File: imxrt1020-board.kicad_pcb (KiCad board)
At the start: 2 copper layers, 102.9 x 68.6 mm, 168 parts, among them J1 Micro_SD_Card_Det, J10 CASTELATED, J11 CASTELATED, J12 CASTELATED, J13 CASTELATED, J14 CASTELATED, J15 CASTELATED, J16 CASTELATED, J17 CASTELATED, J18 CASTELATED, J19 CASTELATED, J2 USB_OTG, J20 CASTELATED, J21 CASTELATED, J22 CASTELATED, J23 CASTELATED, J24 CASTELATED, J25 CASTELATED, J26 CASTELATED, J27 CASTELATED, J28 CASTELATED, J29 CASTELATED, J3 Conn_02x20_Odd_Even, J30 CASTELATED, J31 CASTELATED, J32 CASTELATED, J33 CASTELATED, J34 CASTELATED, J35 CASTELATED, J36 CASTELATED, J37 CASTELATED, J38 CASTELATED, J39 CASTELATED, J4 CASTELATED, J40 CASTELATED, J41 CASTELATED, J42 CASTELATED, J43 CASTELATED, J44 GS2, J45 GS2, J46 PWR_IN, J47 JTAG, J48 Conn_01x05, J49 CASTELATED, J5 CASTELATED, J50 CASTELATED, J51 CASTELATED, J52 CASTELATED, J53 CASTELATED, J54 CASTELATED, J55 CASTELATED, J56 CASTELATED, J57 CASTELATED, J58 RJ45-TRANSFO, J59 CASTELATED, J6 CASTELATED, J60 CASTELATED, J61 CASTELATED, J62 CASTELATED, J63 CASTELATED, J64 CASTELATED, J65 CASTELATED, J66 CASTELATED, J7 CASTELATED, J8 CASTELATED, J9 CASTELATED, SW1 RST, SW2 SW_DIP_x02, U1 imx_rt1020-qfp144, U2 M25PX32-VMW, U3 AS4C16M16S, U4 TPS3839DBZ, U5 LM1084-3.3, U6 ISL3178E, U7 KSZ8081RNA, U8 TCAN332D, Y1 24MHz, Y2 32.768Khz

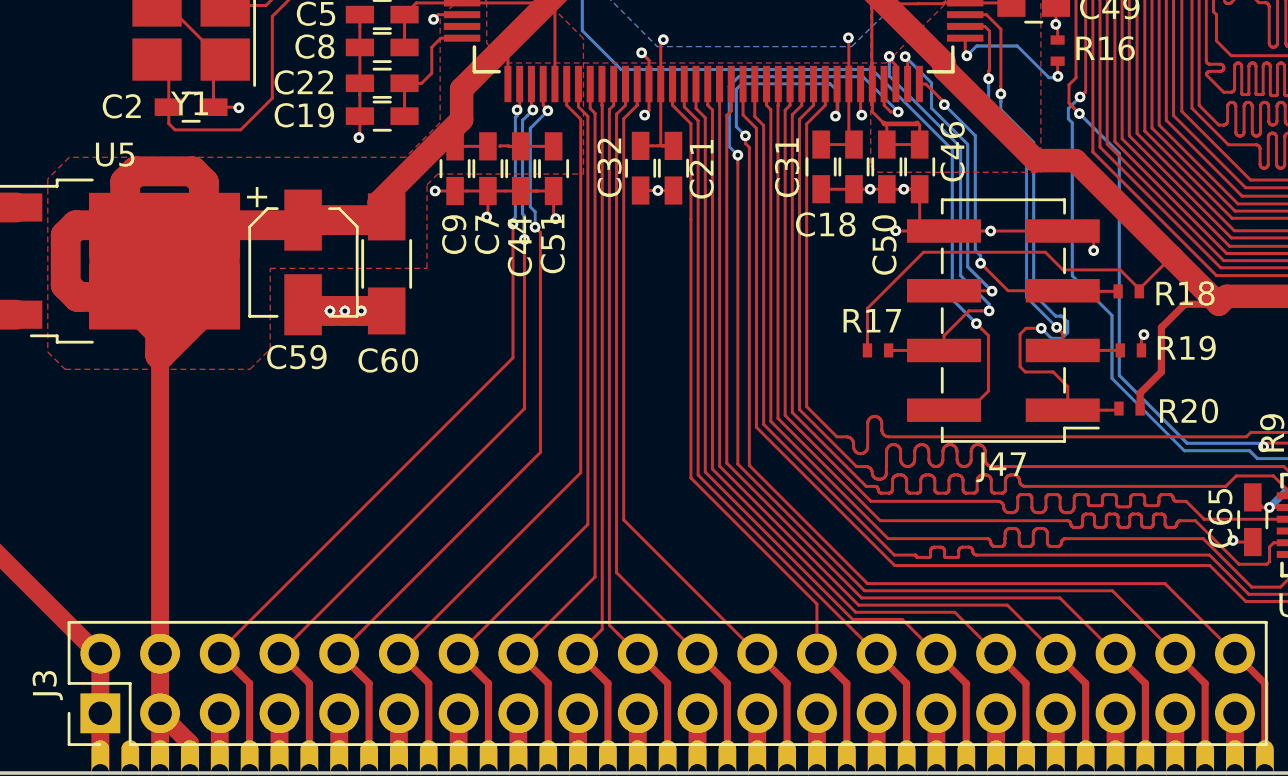
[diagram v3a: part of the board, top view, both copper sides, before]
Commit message: Add GPIO legends (in progress)
Signed-off-by: Martin Ribelotta <martinribelotta@gmail.com>
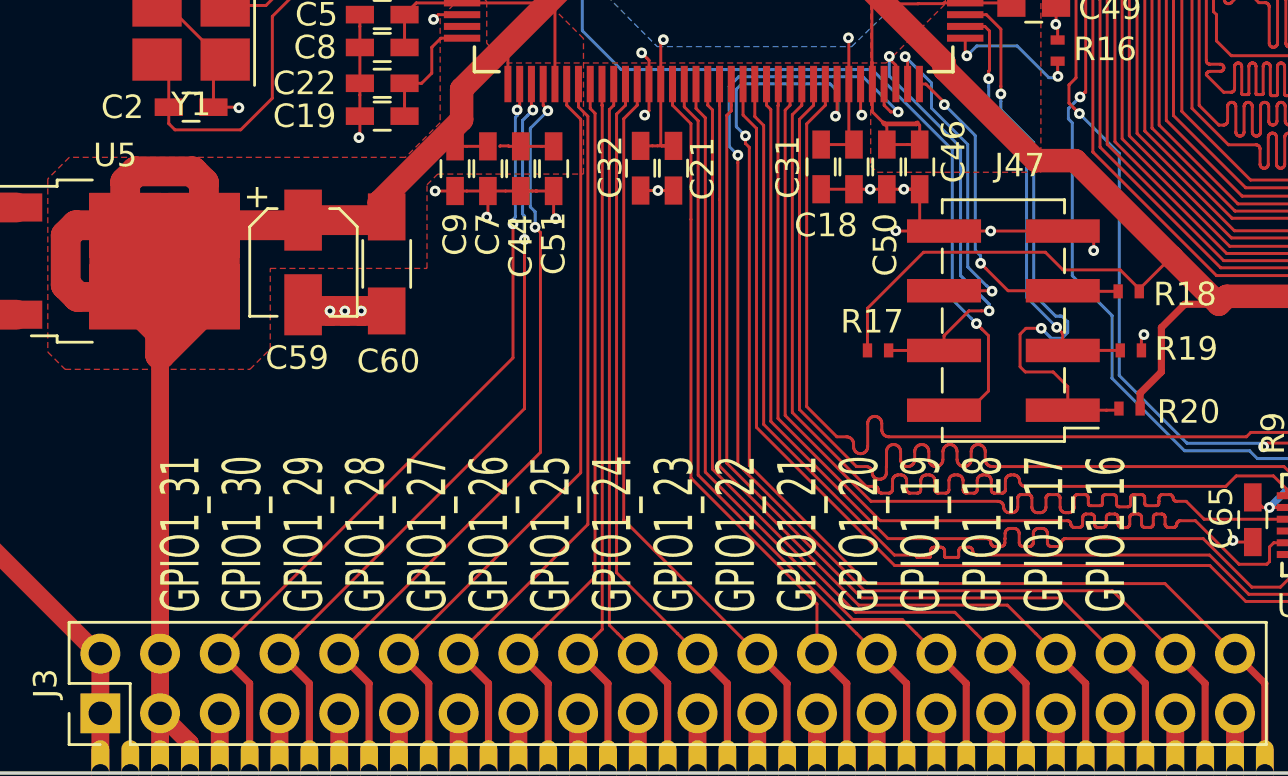
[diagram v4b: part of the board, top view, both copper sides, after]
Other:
- board text added: "GPIO1_31 GPIO1_30 GPIO1_29 GPIO1_28 GPIO1_27 GPIO1_26 GPIO1_25 GPIO1_24 GPIO1_23 GPIO1_22 GPIO1_21 GPIO1_20 GPIO1_19 GPIO1_18 GPIO1_17 GPIO1_16"
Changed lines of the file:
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@@
     (links 461)
     (no_connects 3)
-    (area 107.697199 71.171999 210.72504 139.902001)
+    (area 101.0666 68.199 237.5295 160.624501)
     (thickness 1.6)
-    (drawings 6)
+    (drawings 7)
     (tracks 15178)
     (zones 0)
@@
     (tags "Surface mounted pin header SMD 2x04 2.54mm double row")
     (attr smd)
-    (fp_text reference J47 (at 0 -6.14 180) (layer F.SilkS)
+    (fp_text reference J47 (at -0.69366 6.60146 180) (layer F.SilkS)
       (effects (font (size 1 1) (thickness 0.15)))
     )
@@
     )
   )
+  (gr_text "GPIO1_31\nGPIO1_30\nGPIO1_29\nGPIO1_28\nGPIO1_27\nGPIO1_26\nGPIO1_25\nGPIO1_24\nGPIO1_23\nGPIO1_22\nGPIO1_21\nGPIO1_20\nGPIO1_19\nGPIO1_18\nGPIO1_17\nGPIO1_16\n" (at 151.1935 129.667 90) (layer F.SilkS)
+    (effects (font (size 1.63 1) (thickness 0.25)))
+  )
   (dimension 68.58 (width 0.3) (layer Eco2.User)

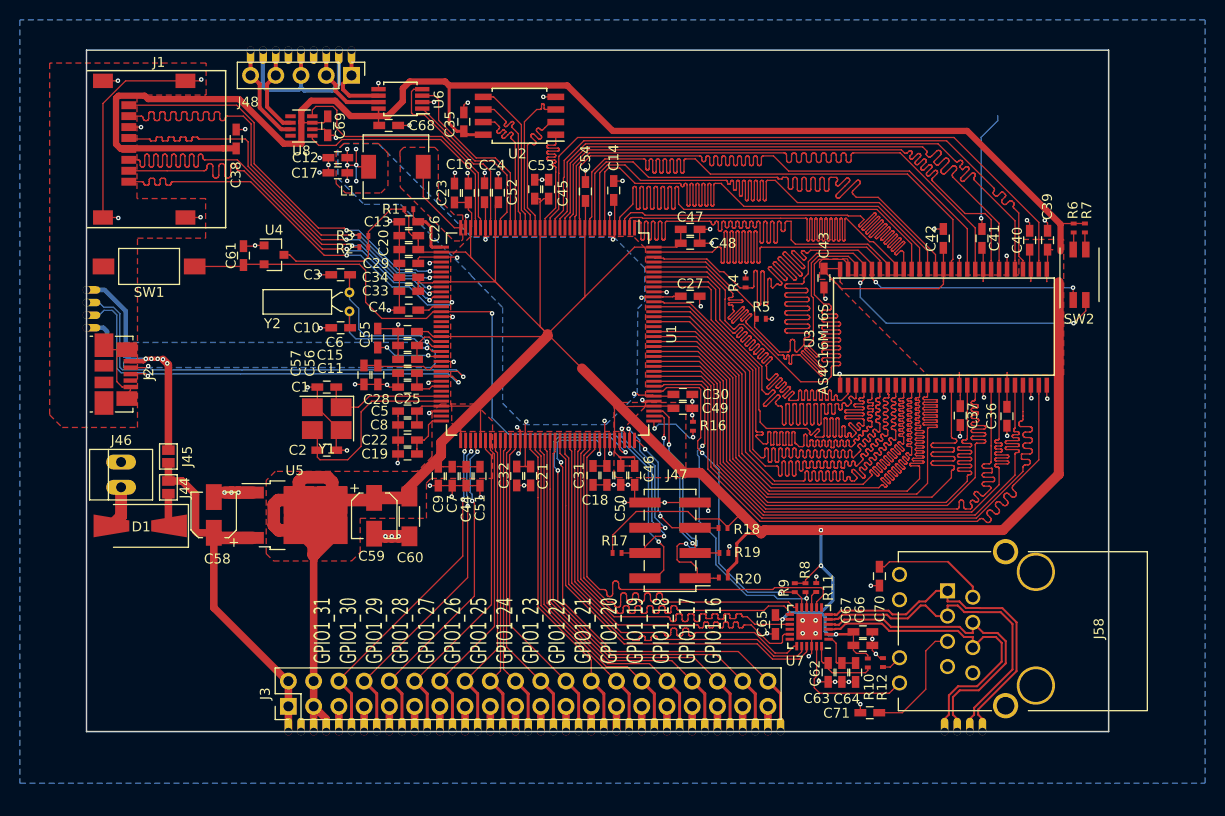
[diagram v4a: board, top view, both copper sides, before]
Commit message: Add WAKE button and GPIO leds, enance GND connections
Signed-off-by: Martin Ribelotta <martinribelotta@gmail.com>
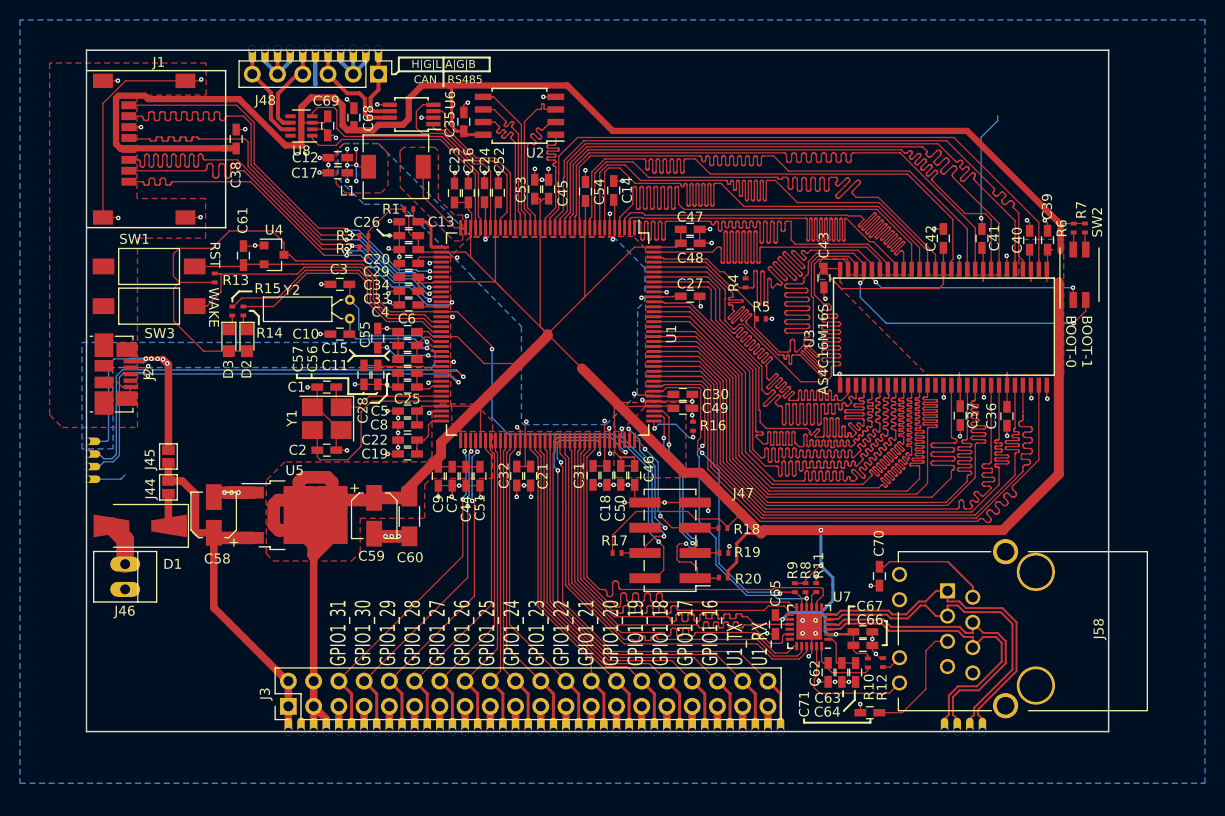
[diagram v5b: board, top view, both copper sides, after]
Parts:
- added D2: RED, LEDs:LED_0805, F.Cu at (123.9, 100.4)
- added D3: RED, LEDs:LED_0805, F.Cu at (122.1, 100.4)
- added J67: CASTELATED, local:castelated_pad, F.Cu at (134.6, 71.1)
- added J68: CASTELATED, local:castelated_pad, F.Cu at (135.9, 71.1)
- added R13: 10K, Resistors_SMD:R_0402_NoSilk, F.Cu at (120.7, 94.2)
- added R14: 220R, Resistors_SMD:R_0402_NoSilk, F.Cu at (123.6, 97.5)
- added R15: 220R, Resistors_SMD:R_0402_NoSilk, F.Cu at (122.4, 97.5)
- added SW3: WAKE, Buttons_Switches_SMD:SW_SPST_FSMSM, F.Cu at (114.1, 97.0)
- J48: value Conn_01x05 -> Conn_01x06; footprint Pin_Headers:Pin_Header_Straight_1x05_Pitch2.54mm -> Pin_Headers:Pin_Header_Straight_1x06_Pitch2.54mm
- moved J65 15.2 mm to (107.8, 110.6)
- moved J66 15.2 mm to (107.8, 114.4)
- moved J63 15.2 mm to (107.8, 113.2)
- moved J64 15.2 mm to (107.8, 111.9)
- moved J46 7.75 mm to (111.7, 123.0), turned to 270 degrees
- moved C68 3.59 mm to (134.7, 78.0), turned to 90 degrees
- moved J49 2.72 mm to (129.5, 71.1)
- moved J48 2.72 mm to (137.2, 73.7)
- moved J55 2.72 mm to (137.2, 71.1)
- moved U6 1.93 mm to (140.5, 77.7)
- moved J52 1.10 mm to (127.0, 71.1)
- moved J53 1.10 mm to (128.3, 71.1)
- moved C3 0.97 mm to (133.3, 94.8)
- moved Y2 0.74 mm to (134.3, 96.4)
- moved C10 0.64 mm to (133.3, 99.8)
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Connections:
- J48 pad 2: /GPIO/RS485_B -> GND
- J48 pad 3: GND -> /GPIO/RS485_B
- J48 pad 5: /GPIO/CAN_H -> GND
- J58 pad GA: /GPIO/ENET_LED0 -> (no net)
- J58 pad GK: Net-(J58-PadGK) -> (no net)
- J58 pad YK: Net-(J58-PadGK) -> Net-(J58-PadYK)
- R12 pad 2: Net-(J58-PadGK) -> Net-(J58-PadYK)
- U1 pad 52: (no net) -> /POWER/WAKEUP
- U1 pad 53: (no net) -> Net-(R15-Pad1)
- U1 pad 54: (no net) -> Net-(R14-Pad1)
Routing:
- net +3V3: track 566.5 -> 601.0 mm
- net /POWER/WAKEUP: track 0.00 -> 31.6 mm
- net Net-(R15-Pad1): track 0.00 -> 26.0 mm
- net Net-(R14-Pad1): track 0.00 -> 24.9 mm
- net GND: track 274.2 -> 285.9 mm, vias 96 -> 111
- net /POWER/PWR_IN1: track 31.7 -> 35.7 mm
- net /GPIO/JTAG_nRST: track 76.0 -> 72.8 mm
- net /GPIO/OTG_D+: track 47.8 -> 50.4 mm
- net /GPIO/OTG_D-: track 48.8 -> 51.4 mm
- net Net-(J58-PadYK): track 0.00 -> 2.45 mm
- net Net-(J58-PadGK): track 2.45 -> 0.00 mm
- net /MEMORY/GPIO3_25: track 18.8 -> 16.6 mm
- net /GPIO/RS485_B: track 9.28 -> 11.4 mm
- net /GPIO/RS485_RX: track 16.9 -> 15.3 mm
- net Net-(D2-Pad1): track 0.00 -> 1.54 mm
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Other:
- board text added: "BOOT-1 BOOT-0"
- board text added: "CAN RS485"
- board text added: "GPIO1_31 GPIO1_30 GPIO1_29 GPIO1_28 GPIO1_27 GPIO1_26 GPIO1_25 GPIO1_24 GPIO1_23 GPIO1_22 GPIO1_21 GPIO1_20 GPIO1_19 GPIO1_18 GPIO1_17 GPIO1_16 U1_TX U1_RX"
- board text added: "H|G|L|A|G|B"
- board text added: "RST"
- board text added: "WAKE"
- board text removed: "GPIO1_31 GPIO1_30 GPIO1_29 GPIO1_28 GPIO1_27 GPIO1_26 GPIO1_25 GPIO1_24 GPIO1_23 GPIO1_22 GPIO1_21 GPIO1_20 GPIO1_19 GPIO1_18 GPIO1_17 GPIO1_16"

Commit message: More GND rework
Signed-off-by: Martin Ribelotta <martinribelotta@gmail.com>
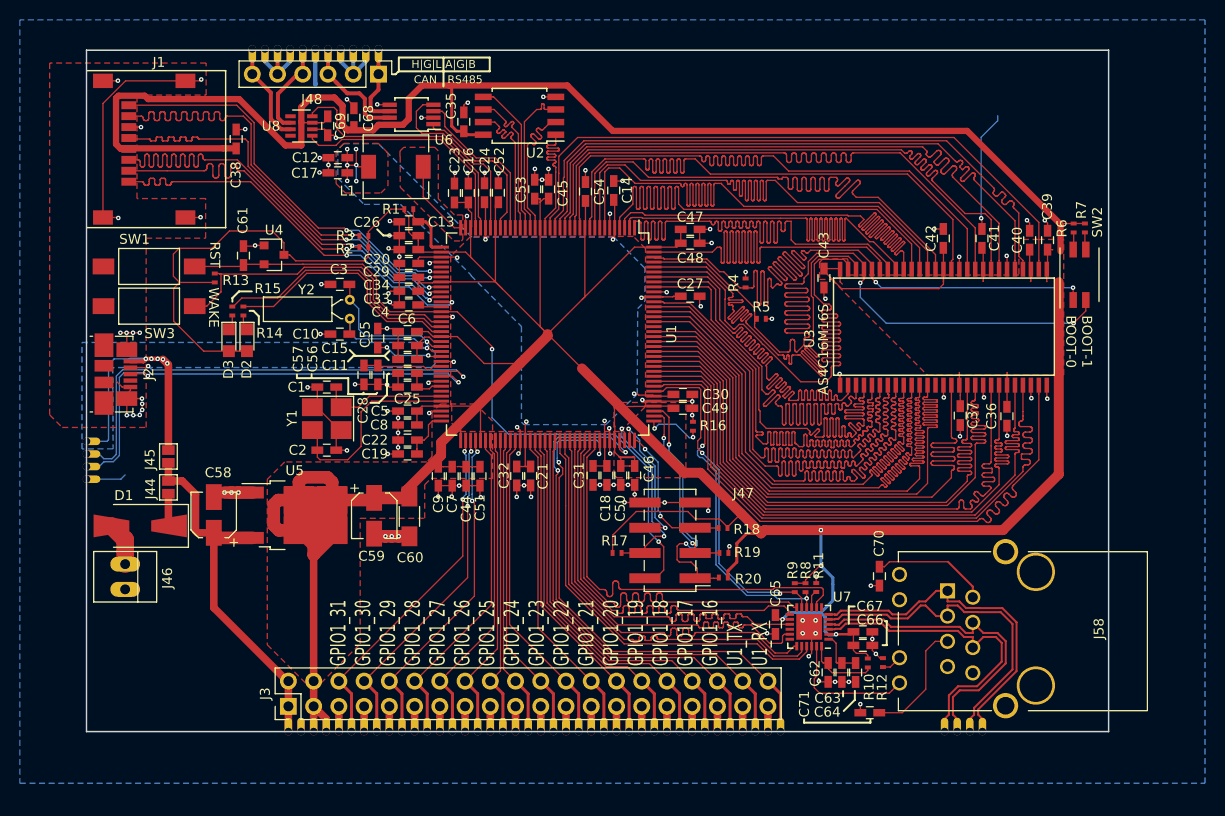
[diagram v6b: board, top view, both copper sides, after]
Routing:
- net GND: track 285.9 -> 295.3 mm, vias 111 -> 122

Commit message: Circuit improves
 - Add power capacitors for PCB sectores (bottom rigth, top left)
 - Add mouting holes
 - Improve castelated and GND planes
 - Improve silkscreen legends
 - Improve puttons/leds possition
 - Improve USB-OTG lines shielding

Signed-off-by: Martin Ribelotta <martinribelotta@gmail.com>
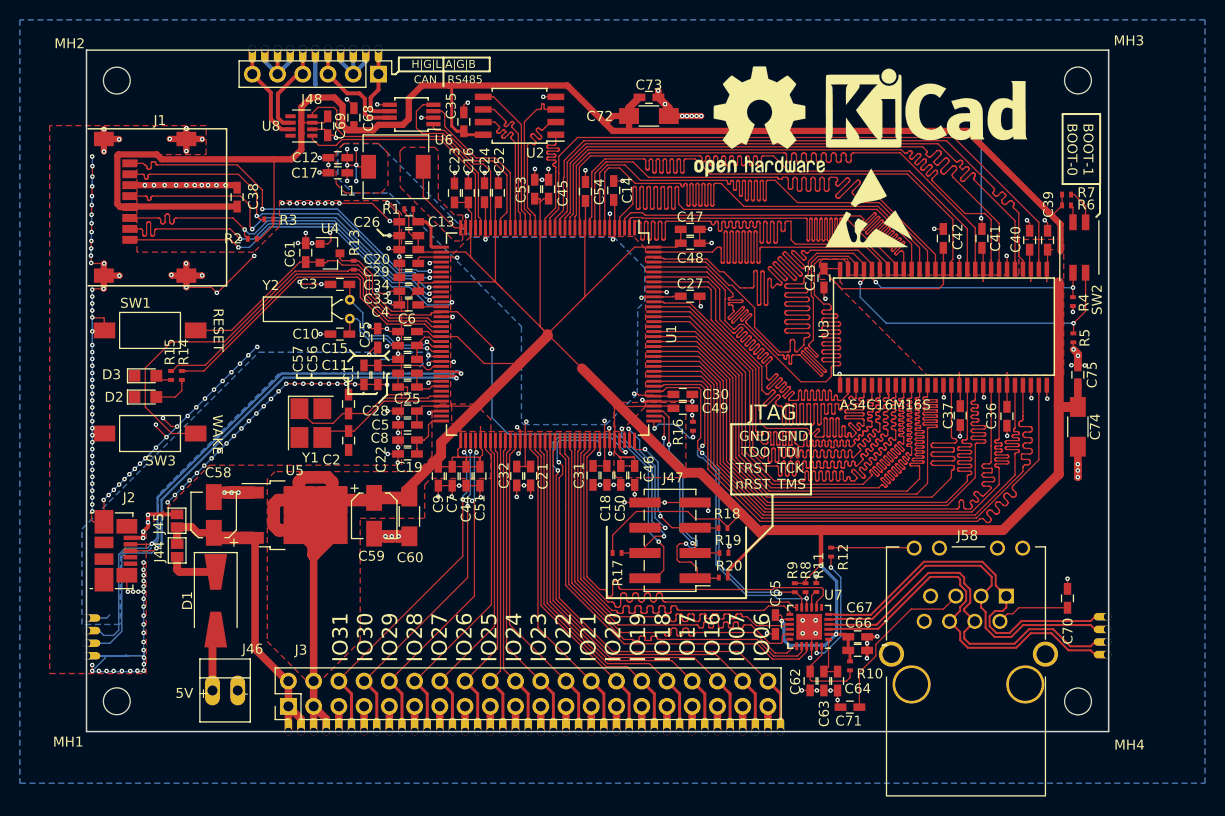
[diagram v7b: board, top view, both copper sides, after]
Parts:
- added C72: 10u, Capacitors_SMD:C_1206_HandSoldering, F.Cu at (164.4, 77.9)
- added C73: 4.7u, Capacitors_SMD:C_0603_HandSoldering, F.Cu at (164.4, 76.0)
- added C74: 10u, Capacitors_SMD:C_1206_HandSoldering, F.Cu at (207.5, 109.2)
- added C75: 4.7u, Capacitors_SMD:C_0603_HandSoldering, F.Cu at (207.5, 103.9)
- added MH1: HOLE, Mounting_Holes:MountingHole_2.7mm_M2.5, F.Cu at (110.8, 136.8)
- added MH2: HOLE, Mounting_Holes:MountingHole_2.7mm_M2.5, F.Cu at (110.8, 74.3)
- added MH3: HOLE, Mounting_Holes:MountingHole_2.7mm_M2.5, F.Cu at (207.6, 74.3)
- added MH4: HOLE, Mounting_Holes:MountingHole_2.7mm_M2.5, F.Cu at (207.6, 136.8)
- added REF***: ESD-Logo_8.9x8mm_SilkScreen, Symbols:ESD-Logo_8.9x8mm_SilkScreen, F.Cu at (186.5, 87.1)
- added REF***: KiCad-Logo_8mm_SilkScreen, Symbols:KiCad-Logo_8mm_SilkScreen, F.Cu at (192.3, 77.1)
- added REF***: OSHW-Logo2_14.6x12mm_SilkScreen, Symbols:OSHW-Logo2_14.6x12mm_SilkScreen, F.Cu at (175.5, 78.4)
- moved R4 33.0 mm to (207.1, 96.6), turned to 270 degrees
- moved R5 31.5 mm to (207.1, 100.2), turned to 270 degrees
- moved C70 19.1 mm to (206.5, 126.4), turned to 90 degrees
- moved J62 18.1 mm to (210.5, 132.1), turned to 90 degrees
- moved J63 17.8 mm to (107.8, 130.9)
- moved J2 17.8 mm to (109.5, 121.6)
- moved J64 17.8 mm to (107.8, 129.7)
- moved J65 17.8 mm to (107.8, 128.4)
- moved J66 17.8 mm to (107.8, 132.2)
- moved J61 17.6 mm to (210.5, 130.8), turned to 90 degrees
- moved J60 17.3 mm to (210.5, 129.5), turned to 90 degrees
- moved J59 17.1 mm to (210.5, 128.3), turned to 90 degrees
- moved J46 15.5 mm to (120.5, 135.7), turned to 0 degrees
- moved R13 14.1 mm to (134.7, 92.9), turned to 90 degrees
- moved SW3 12.8 mm to (114.2, 109.8)
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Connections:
- D2 pad 1: Net-(D2-Pad1) -> GND
- D2 pad 2: +3V3 -> Net-(D2-Pad2)
- D3 pad 1: Net-(D3-Pad1) -> GND
- D3 pad 2: +3V3 -> Net-(D3-Pad2)
- J58 pad YA: /GPIO/ENET_LED0 -> Net-(J58-PadYA)
- J58 pad YK: Net-(J58-PadYK) -> GND
- R12 pad 1: GND -> Net-(R12-Pad1)
- R12 pad 2: Net-(J58-PadYK) -> Net-(J58-PadYA)
- R14 pad 2: Net-(D2-Pad1) -> Net-(D2-Pad2)
- R15 pad 2: Net-(D3-Pad1) -> Net-(D3-Pad2)
- U7 pad 23: /GPIO/ENET_LED0 -> Net-(R12-Pad1)
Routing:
- net GND: track 295.3 -> 451.0 mm, vias 122 -> 284
- net /POWER/PWR_IN1: track 35.7 -> 12.0 mm, vias 7 -> 6
- net /POWER/WAKEUP: track 31.6 -> 47.2 mm
- net /MEMORY/SD_CMD: track 53.3 -> 39.1 mm
- net /GPIO/ENET_LED0: track 13.5 -> 0.00 mm
- net /MEMORY/SD_D0: track 51.8 -> 38.9 mm
- net +3V3: track 601.0 -> 588.6 mm, vias 4 -> 3
- net Net-(R12-Pad1): track 0.00 -> 12.3 mm, vias 0 -> 2
- net /GPIO/OTG_D+: track 50.4 -> 59.8 mm
- net /GPIO/OTG_D-: track 51.4 -> 60.1 mm
- net Net-(R14-Pad1): track 24.9 -> 33.3 mm
- net Net-(R15-Pad1): track 26.0 -> 34.5 mm
- net Net-(J58-PadYA): track 0.00 -> 8.38 mm
- net /GPIO/ENET_RX-: track 32.4 -> 39.7 mm
- net /GPIO/ENET_RX+: track 33.1 -> 39.7 mm
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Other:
- board text added: "5V + -"
- board text added: "GND TDI TCK TMS"
- board text added: "GND TDO TRST nRST"
- board text added: "IO31 IO30 IO29 IO28 IO27 IO26 IO25 IO24 IO23 IO22 IO21 IO20 IO19 IO18 IO17 IO16 IO07 IO06"
- board text added: "JTAG"
- board text added: "RESET"
- board text removed: "GPIO1_31 GPIO1_30 GPIO1_29 GPIO1_28 GPIO1_27 GPIO1_26 GPIO1_25 GPIO1_24 GPIO1_23 GPIO1_22 GPIO1_21 GPIO1_20 GPIO1_19 GPIO1_18 GPIO1_17 GPIO1_16 U1_TX U1_RX"
- board text removed: "RST"
